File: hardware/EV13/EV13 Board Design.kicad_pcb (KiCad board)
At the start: 4 copper layers, 66 x 99.3 mm, 129 parts, among them CN2 Conn_05x02_Female, CN3 Conn_01x06_Female, CN4 Conn_01x06_Female, CN5 Conn_02x05_Male, CN6 Conn_02x05_Male, CN7 Conn_02x05_Male, J1 Conn_01x02_Socket, J10 Conn_01x08_Socket, J2 AudioJack1, J3 Conn_01x06_Socket, J9 USB_C_Receptacle, SW1 TS-1037-A11B3-D2, SW3 TS-1037-A11B3-D2, SW4 SW_Push, SW5 SW_Push, SW6 SW_SPDT, U1 STM32F405RGTx, U11 ESP32-S3-WROOM-1-N8R2, U13 BM14B(0.8)-24DS-0.4V(53), U2 BQ21040DBV, U3 CH340C, U4 USBLC6-2P6, U5 M24C02-RMN6TP, U6 WM8960CGEFL/RV, U7 TPS63060, U8 STM32F072CBTx, Y1 Crystal_GND24

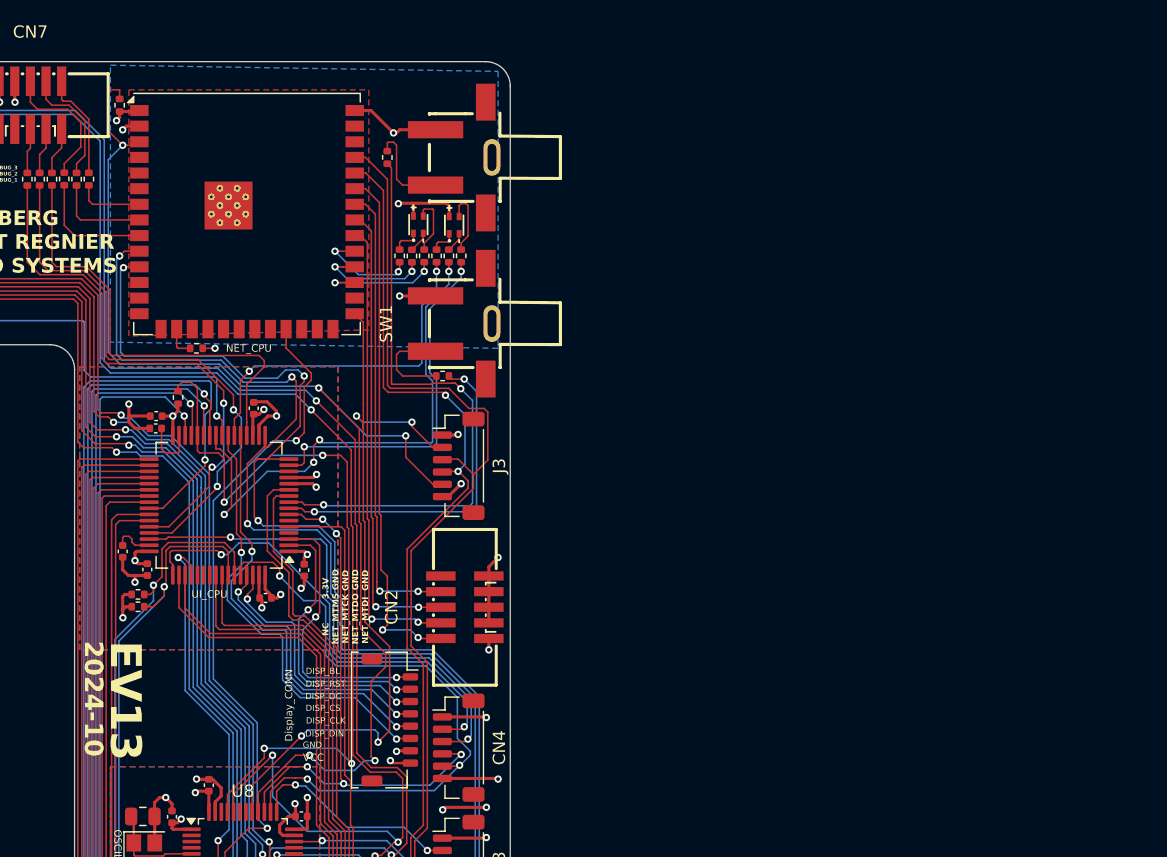
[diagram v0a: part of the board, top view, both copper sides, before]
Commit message: Replaced side buttons, updated capacitor part #, removed extra 1k resistor, switched connectors to new part #
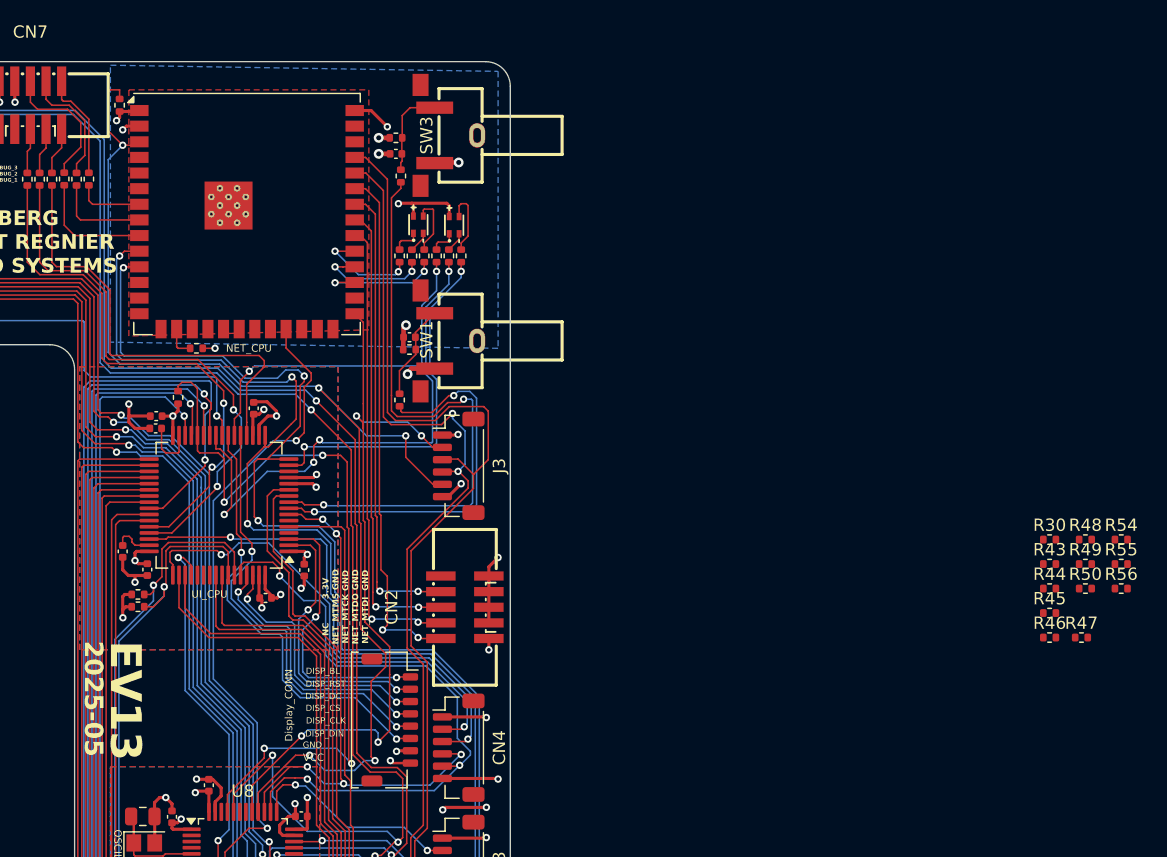
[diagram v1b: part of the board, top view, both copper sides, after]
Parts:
- removed R29: 1k0, Resistor_SMD:R_0402_1005Metric
- added C22: 100n, Capacitor_SMD:C_0402_1005Metric, F.Cu at (170.7, 53.5)
- added C27: 100n, Capacitor_SMD:C_0402_1005Metric, F.Cu at (171.8, 68.4)
- added R30: 4k7, Resistor_SMD:R_0402_1005Metric, F.Cu at (223.8, 84.8)
- added R43: 4k7, Resistor_SMD:R_0402_1005Metric, F.Cu at (223.8, 86.8)
- added R44: 4k7, Resistor_SMD:R_0402_1005Metric, F.Cu at (223.8, 88.8)
- added R45: 4k7, Resistor_SMD:R_0402_1005Metric, F.Cu at (223.8, 90.8)
- added R46: 4k7, Resistor_SMD:R_0402_1005Metric, F.Cu at (223.8, 92.8)
- added R47: 4k7, Resistor_SMD:R_0402_1005Metric, F.Cu at (226.4, 92.8)
- added R48: 4k7, Resistor_SMD:R_0402_1005Metric, F.Cu at (226.7, 84.8)
- added R49: 4k7, Resistor_SMD:R_0402_1005Metric, F.Cu at (226.7, 86.8)
- added R50: 47k, Resistor_SMD:R_0402_1005Metric, F.Cu at (226.7, 88.8)
- added R51: 1k0, Resistor_SMD:R_0402_1005Metric, F.Cu at (171.1, 55.3)
- added R52: 4k7, Resistor_SMD:R_0402_1005Metric, F.Cu at (171.8, 69.4)
- added R53: 4k7, Resistor_SMD:R_0402_1005Metric, F.Cu at (170.7, 52.2)
- added R54: 4k7, Resistor_SMD:R_0402_1005Metric, F.Cu at (229.6, 84.8)
- added R55: 4k7, Resistor_SMD:R_0402_1005Metric, F.Cu at (229.6, 86.8)
- added R56: 4k7, Resistor_SMD:R_0402_1005Metric, F.Cu at (229.6, 88.8)
- SW1, SW3: value TS-1037-A11B3-D2 -> SW_Push; footprint Hactar_Footprints:KEY-SMD_2P-L7.1-W10.6-P4.00-LS9.0 -> Hactar_Footprints:SW-SMD_L7.5-W8.0-P4.50_TS-1045-A13B3-D2
- moved R28 4.00 mm to (171.0, 73.5), turned to 90 degrees
- moved SW3 2.17 mm to (175.0, 52.0)
- moved SW1 1.85 mm to (175.0, 68.7)
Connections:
- R28 pad 1: Net-(U1-PC0) -> /PTT_BTN
- R28 pad 2: /PTT_BTN -> Net-(C27-Pad1)
- SW1 pad 1: /PTT_BTN -> +3.3V
- SW1 pad 2: GND -> Net-(C27-Pad1)
- SW3 pad 1: /PTT_AI_BTN -> +3.3V
- SW3 pad 2: GND -> Net-(C22-Pad1)
- U1 pad 10: /USB_CC2_DETECT -> unconnected-(U1-PC2-Pad10)
- U1 pad 11: /USB_CC1_DETECT -> unconnected-(U1-PC3-Pad11)
- U1 pad 14: /Wake up Pin -> /UI_CTS2_NET
- U1 pad 15: /UI_LED_B -> /UI_RTS2_NET
- U1 pad 4: unconnected-(U1-PC15-Pad4) -> /UI_DEBUG_1
- U1 pad 44: /UI_DEBUG_1 -> /UI_CTS1_MGMT
- U1 pad 45: /UI_DEBUG_2 -> /UI_RTS1_MGMT
- U1 pad 54: unconnected-(U1-PD2-Pad54) -> /UI_DEBUG_2
- U1 pad 55: unconnected-(U1-PB3-Pad55) -> /UI_LED_B
- U1 pad 8: Net-(U1-PC0) -> /PTT_BTN
- U1 pad 9: Net-(U1-PC1) -> /PTT_AI_BTN
- U11 pad 13: unconnected-(U11-IO19-Pad13) -> /UI_RTS2_NET
- U11 pad 14: unconnected-(U11-IO20-Pad14) -> /UI_CTS2_NET
- U11 pad 5: unconnected-(U11-IO5-Pad5) -> /NET_DEBUG_1
- U11 pad 6: unconnected-(U11-IO6-Pad6) -> /NET_DEBUG_2
- U11 pad 7: /NET_DEBUG_1 -> /NET_DEBUG_3
- U11 pad 8: /NET_DEBUG_2 -> /NET_RTS1_MGMT
- U11 pad 9: /NET_DEBUG_3 -> /NET_CTS1_MGMT
- U13 pad 23: /KB_LED -> GND
- U13 pad 24: /KB_LED -> GND
- U13 pad 25: /KB_LED -> GND
- U13 pad 26: /KB_LED -> GND
- U3 pad 13: /USB_DTR -> /USB_DTR_MGMT
- U3 pad 14: /USB_RTS -> /USB_RTS_MGMT
- U3 pad 9: unconnected-(U3-~{CTS}-Pad9) -> /USB_CTS_MGMT
- U6 pad 2: unconnected-(U6-LINPUT3-Pad2) -> GNDA
- U6 pad 5: unconnected-(U6-RINPUT1-Pad5) -> GNDA
- U6 pad 6: unconnected-(U6-RINPUT2-Pad6) -> GNDA
- U6 pad 7: unconnected-(U6-RINPUT3-Pad7) -> GNDA
- U8 pad 10: /UI_STAT -> /UI_RTS1_MGMT
- U8 pad 11: /NET_STAT -> /UI_CTS1_MGMT
- U8 pad 19: /USB_RTS -> unconnected-(U8-PB1-Pad19)
- U8 pad 20: unconnected-(U8-PB2-Pad20) -> /USB_DTR_MGMT
- U8 pad 26: /USB_DTR -> /NET_CTS1_MGMT
- U8 pad 27: /LEDB_G -> /NET_RTS1_MGMT
- U8 pad 3: unconnected-(U8-PC14-Pad3) -> /USB_CC2_DETECT
- U8 pad 32: unconnected-(U8-PA11-Pad32) -> /USB_CTS_MGMT
- U8 pad 33: unconnected-(U8-PA12-Pad33) -> /USB_RTS_MGMT
- U8 pad 4: unconnected-(U8-PC15-Pad4) -> /USB_CC1_DETECT
- U8 pad 42: unconnected-(U8-PB6-Pad42) -> /LEDB_G
- U8 pad 43: unconnected-(U8-PB7-Pad43) -> /NET_STAT
- U8 pad 46: unconnected-(U8-PB9-Pad46) -> /UI_STAT
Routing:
- net (no net): track 0.00 -> 64.4 mm, vias 0 -> 6
- net Net-(U1-PC1): track 48.7 -> 0.00 mm, vias 2 -> 0
- net /PTT_AI_BTN: track 7.66 -> 50.0 mm, vias 0 -> 2
- net /USB_DTR: track 35.1 -> 0.00 mm, vias 4 -> 0
- net /USB_RTS: track 29.3 -> 0.00 mm, vias 2 -> 0
- net Net-(U1-PC0): track 27.7 -> 0.00 mm, vias 2 -> 0
- net /PTT_BTN: track 7.96 -> 31.9 mm, vias 0 -> 2
- net +3.3V: track 498.5 -> 511.8 mm, vias 35 -> 37
- net Net-(C27-Pad1): track 0.00 -> 7.80 mm
- net Net-(C22-Pad1): track 0.00 -> 7.37 mm
- net /NET_TX1_MGMT: track 100.0 -> 102.3 mm
- net GND: track 618.5 -> 616.6 mm, vias 73 -> 75
- net /NET_RX1_MGMT: track 97.7 -> 99.3 mm
- net unconnected-(U8-PA12-Pad33): track 0.50 -> 0.00 mm
- net /USB_RTS_MGMT: track 0.00 -> 0.50 mm
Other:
- board text added: "2025-05"
- board text removed: "2024-10"

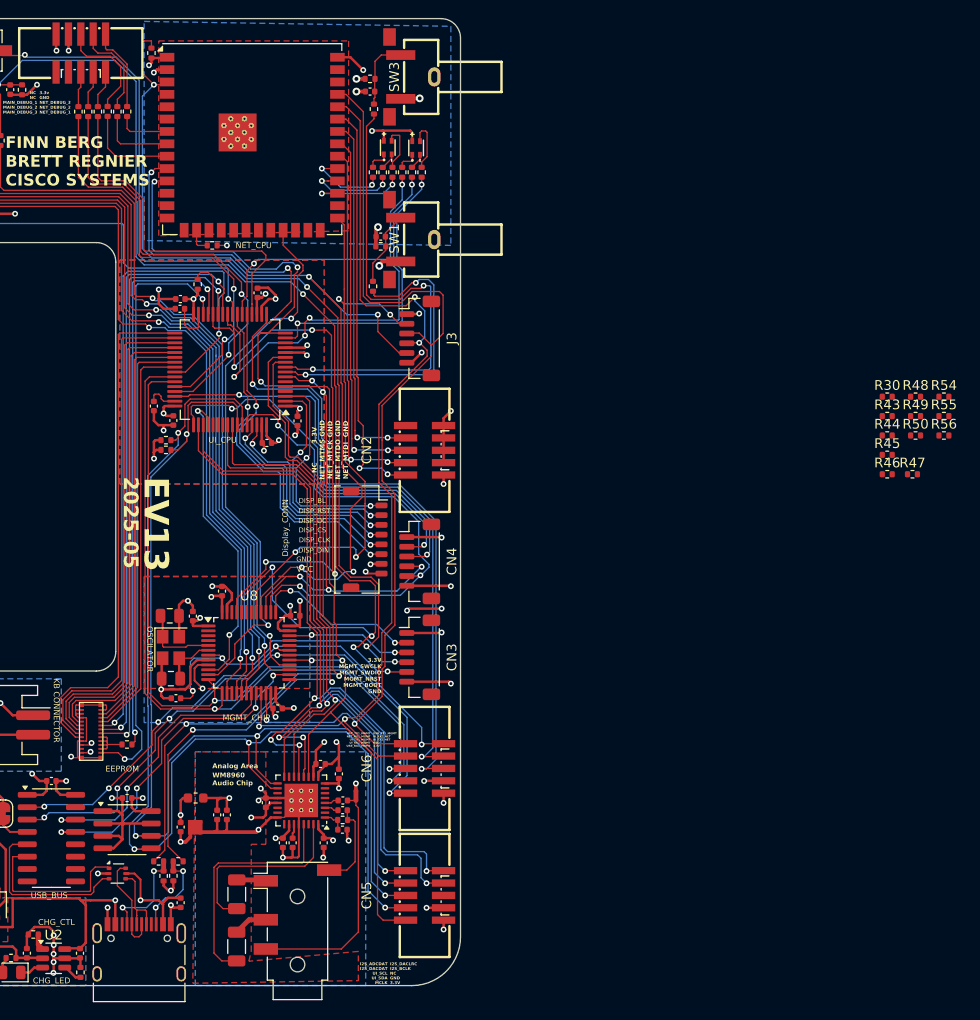
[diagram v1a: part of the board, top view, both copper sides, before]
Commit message: Connected extra pull down resistors and removed incorrect previous traces
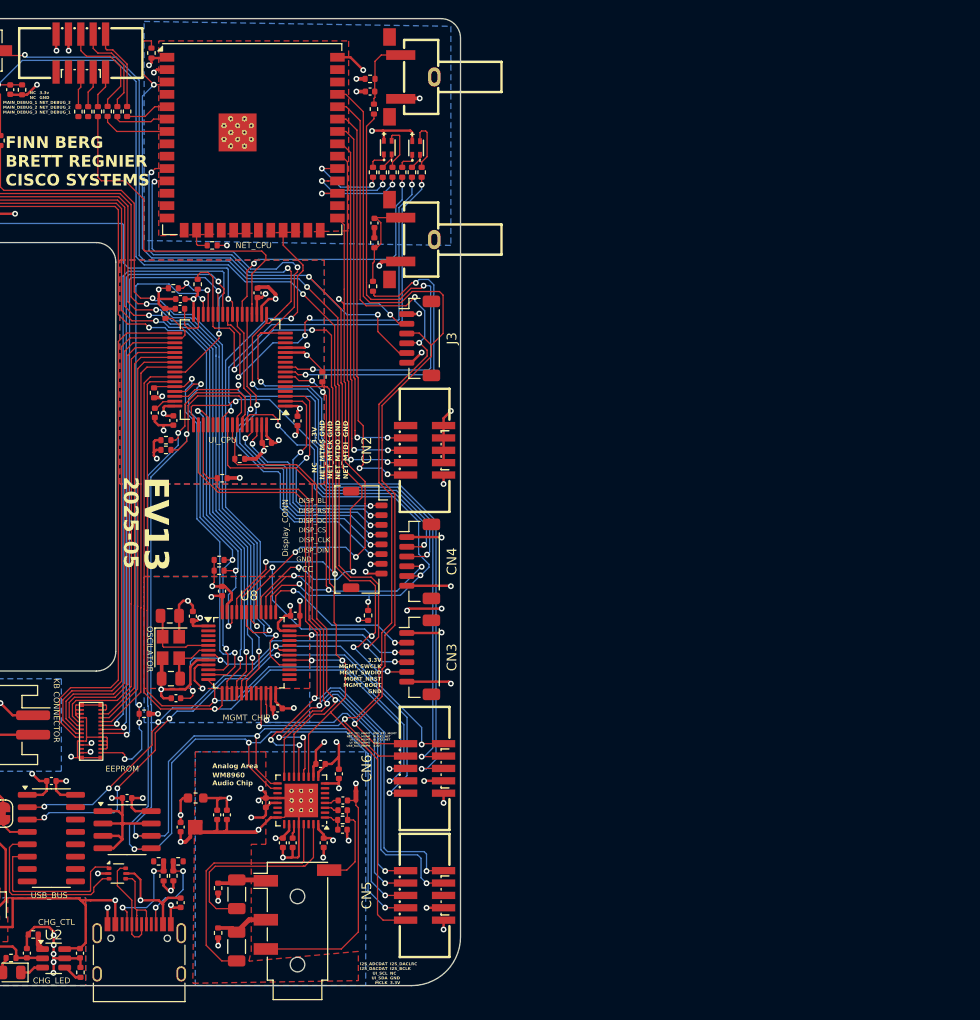
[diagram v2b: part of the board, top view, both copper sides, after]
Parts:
- removed the R30 at (145.8, 120.5)
- moved R56 90.4 mm to (155.1, 139.9), turned to 90 degrees
- moved R55 88.9 mm to (155.1, 135.3), turned to 90 degrees
- moved R44 81.5 mm to (147.5, 117.4), turned to 180 degrees
- moved R47 78.5 mm to (149.7, 76.3), turned to -90 degrees
- moved R49 78.2 mm to (148.5, 84.4), turned to 90 degrees
- moved R43 74.5 mm to (150.5, 73.7)
- moved R48 73.5 mm to (155.2, 101.6)
- moved R45 69.6 mm to (155.2, 102.7)
- moved R30 68.8 mm to (155.5, 93.2), turned to 180 degrees
- moved R46 66.5 mm to (157.3, 91.2), turned to 180 degrees
- moved R54 63.3 mm to (170.5, 107.3), turned to -90 degrees
- moved R50 61.2 mm to (165.8, 82.8), turned to -90 degrees
- moved C27 1.54 mm to (171.2, 67.0), turned to -90 degrees
- moved R52 0.76 mm to (171.2, 69.0), turned to -90 degrees
- moved C19 0.71 mm to (148.6, 86.5)
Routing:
- net /USB_CC2_DETECT: track 70.0 -> 0.00 mm, vias 2 -> 0
- net /USB_CC1_DETECT: track 69.8 -> 0.00 mm, vias 2 -> 0
- net (no net): track 64.4 -> 0.00 mm, vias 6 -> 0
- net Net-(U1-PB10): track 58.4 -> 6.12 mm
- net /UI_DEBUG_2: track 45.2 -> 0.00 mm, vias 2 -> 0
- net /UI_DEBUG_1: track 44.3 -> 0.00 mm, vias 2 -> 0
- net /UI_CTS1_MGMT: track 0.00 -> 40.3 mm, vias 0 -> 2
- net /UI_RTS1_MGMT: track 0.00 -> 37.8 mm, vias 0 -> 3
- net GND: track 616.6 -> 645.5 mm, vias 75 -> 78
- net GNDA: track 75.2 -> 89.7 mm, vias 8 -> 10
- net /UI_LED_B: track 29.5 -> 41.8 mm
- net /KB_LED: track 5.51 -> 0.00 mm
- net /LEDB_G: track 77.6 -> 72.3 mm
- net /NET_STAT: track 57.1 -> 52.8 mm
- net /KB_COL1: track 52.0 -> 55.8 mm
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
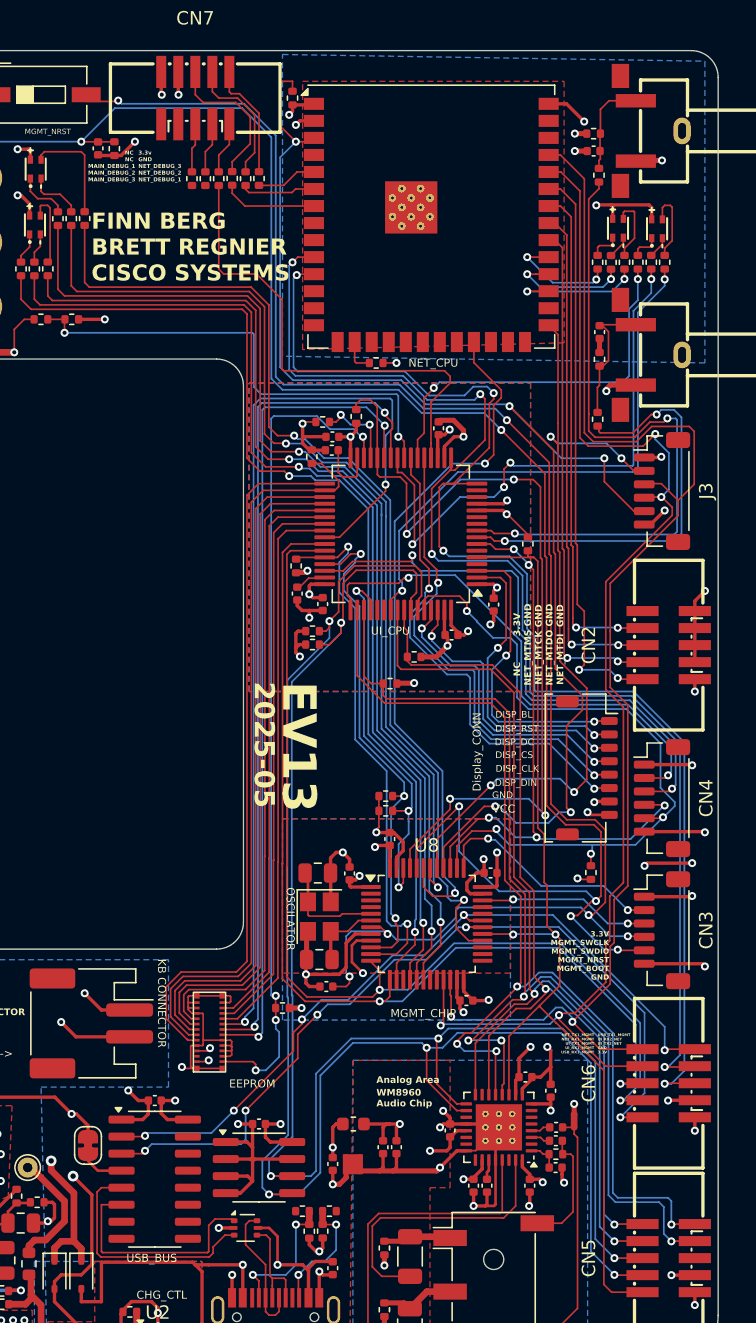
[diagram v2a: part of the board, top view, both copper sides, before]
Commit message: cleaned up and connected missing traces
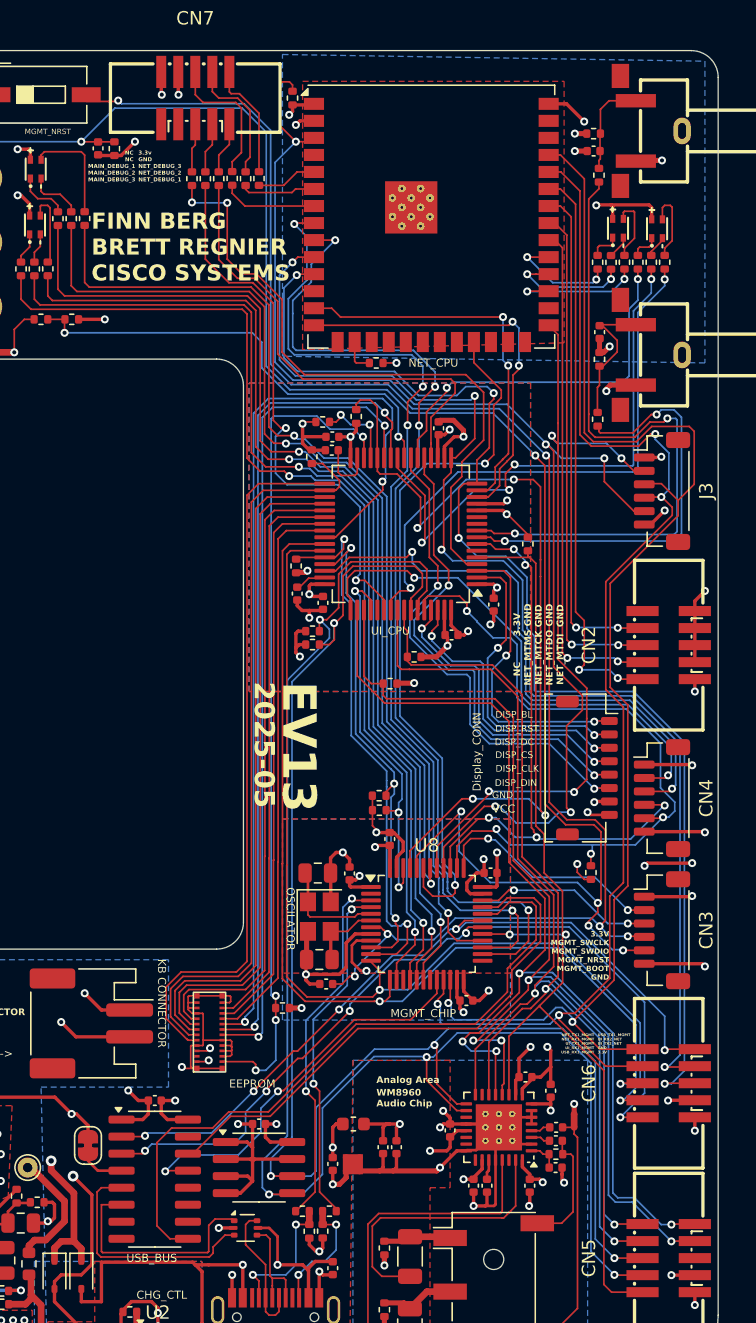
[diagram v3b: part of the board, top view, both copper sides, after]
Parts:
- moved R48 0.49 mm to (154.7, 101.6)
- moved R45 0.48 mm to (154.7, 102.6)
- moved C35 0.19 mm to (150.8, 115.6)
- moved C13 0.09 mm to (150.5, 87.2)
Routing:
- net /NET_CTS1_MGMT: track 0.00 -> 76.5 mm, vias 0 -> 4
- net /NET_RTS1_MGMT: track 0.00 -> 75.2 mm, vias 0 -> 4
- net /USB_CTS_MGMT: track 0.00 -> 51.4 mm
- net /UI_DEBUG_1: track 0.00 -> 48.7 mm, vias 0 -> 2
- net /UI_DEBUG_2: track 0.00 -> 42.0 mm, vias 0 -> 2
- net /USB_RTS_MGMT: track 0.50 -> 41.9 mm
- net /UI_CTS2_NET: track 0.00 -> 30.0 mm, vias 0 -> 2
- net /USB_DTR_MGMT: track 0.00 -> 29.5 mm, vias 0 -> 2
- net /UI_RTS2_NET: track 0.00 -> 28.9 mm, vias 0 -> 2
- net /USB_CC2_DETECT: track 0.00 -> 27.1 mm, vias 0 -> 2
- net /USB_CC1_DETECT: track 0.00 -> 25.9 mm, vias 0 -> 2
- net GNDA: track 89.7 -> 97.8 mm
- net /UI_TX2_NET: track 98.4 -> 94.0 mm
- net /NET_NRST: track 104.2 -> 100.5 mm
- net GND: track 645.5 -> 648.8 mm, vias 78 -> 79
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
